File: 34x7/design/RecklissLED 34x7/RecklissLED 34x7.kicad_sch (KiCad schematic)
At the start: 6 parts

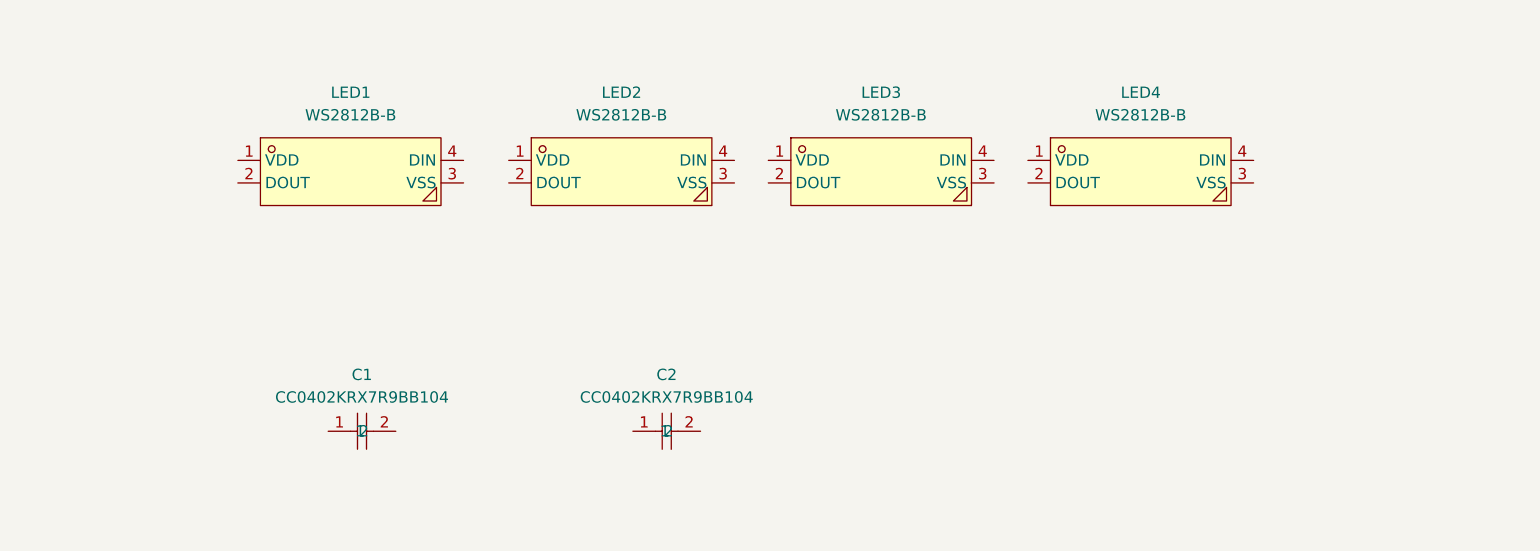
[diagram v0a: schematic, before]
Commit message: Added solder pads, began schematic routing, components consolidated on pcb.
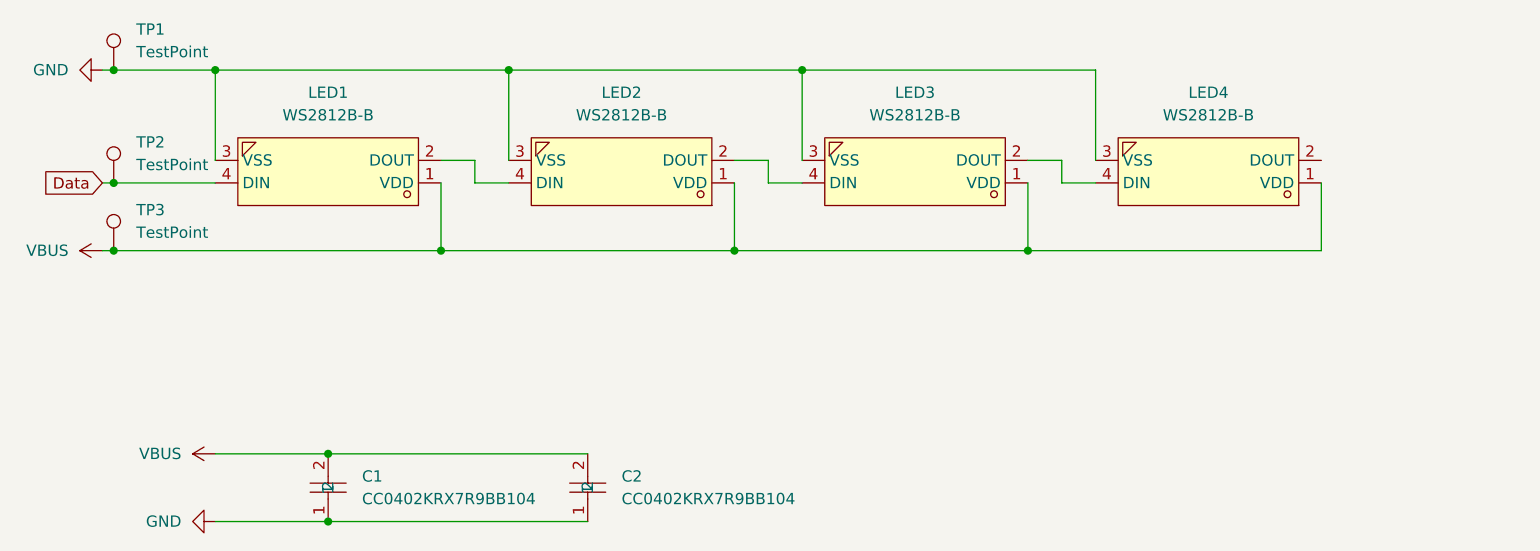
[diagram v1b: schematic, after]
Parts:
- added TP1, TP2, TP3: TestPoint, Connector_Wire:SolderWirePad_1x01_SMD_1x2mm, symbol Connector:TestPoint
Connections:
- net VBUS: now reaches LED3.1 (VDD)
- net VBUS: now also C1.2, C2.2, LED1.1 (VDD), LED2.1 (VDD), LED4.1 (VDD), TP3.1
- net at LED3.2 (DOUT): now also LED4.4 (DIN)
- net GND: now reaches LED3.3 (VSS)
- net GND: now also C1.1, C2.1, LED1.3 (VSS), LED2.3 (VSS), LED4.3 (VSS), TP1.1
- net at LED3.4 (DIN): now also LED2.2 (DOUT)
- net at LED2.4 (DIN): now also LED1.2 (DOUT)
- net Data: now reaches LED1.4 (DIN)
- net Data: now also TP2.1
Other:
- moved on the sheet: C1, C2, LED1, LED2, LED3, LED4

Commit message: Update schematic and pcb routing.
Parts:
- added TP4, TP5, TP6: TestPoint, Connector_Wire:SolderWirePad_1x01_SMD_1x2mm, symbol Connector:TestPoint
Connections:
- net GND: now also TP4.1
- net VBUS: now also TP6.1
- net at LED4.2 (DOUT): now also TP5.1
